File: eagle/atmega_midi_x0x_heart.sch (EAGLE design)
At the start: 31 parts, among them IC1 TL072P, J11_VCF_CUTOFF 22-23-2021, U1 ATMEGA328P_PDIP

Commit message: nearly routed
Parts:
- C1, C2: device rcl:C-US025-040X050 -> rcl:C-US050-024X044
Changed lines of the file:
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@@
 <grid distance="0.1" unitdist="inch" unit="inch" style="lines" multiple="1" display="no" altdistance="0.01" altunitdist="inch" altunit="inch"/>
 <layers>
-<layer number="1" name="Top" color="4" fill="1" visible="no" active="no"/>
-<layer number="16" name="Bottom" color="1" fill="1" visible="no" active="no"/>
-<layer number="17" name="Pads" color="2" fill="1" visible="no" active="no"/>
-<layer number="18" name="Vias" color="2" fill="1" visible="no" active="no"/>
-<layer number="19" name="Unrouted" color="6" fill="1" visible="no" active="no"/>
-<layer number="20" name="Dimension" color="15" fill="1" visible="no" active="no"/>
-<layer number="21" name="tPlace" color="7" fill="1" visible="no" active="no"/>
-<layer number="22" name="bPlace" color="7" fill="1" visible="no" active="no"/>
-<layer number="23" name="tOrigins" color="15" fill="1" visible="no" active="no"/>
-<layer number="24" name="bOrigins" color="15" fill="1" visible="no" active="no"/>
-<layer number="25" name="tNames" color="7" fill="1" visible="no" active="no"/>
-<layer number="26" name="bNames" color="7" fill="1" visible="no" active="no"/>
-<layer number="27" name="tValues" color="7" fill="1" visible="no" active="no"/>
-<layer number="28" name="bValues" color="7" fill="1" visible="no" active="no"/>
+<layer number="1" name="Top" color="4" fill="1" visible="yes" active="no"/>
+<layer number="16" name="Bottom" color="1" fill="1" visible="yes" active="no"/>
+<layer number="17" name="Pads" color="2" fill="1" visible="yes" active="no"/>
+<layer number="18" name="Vias" color="2" fill="1" visible="yes" active="no"/>
+<layer number="19" name="Unrouted" color="6" fill="1" visible="yes" active="no"/>
+<layer number="20" name="Dimension" color="15" fill="1" visible="yes" active="no"/>
+<layer number="21" name="tPlace" color="7" fill="1" visible="yes" active="no"/>
+<layer number="22" name="bPlace" color="7" fill="1" visible="yes" active="no"/>
+<layer number="23" name="tOrigins" color="15" fill="1" visible="yes" active="no"/>
+<layer number="24" name="bOrigins" color="15" fill="1" visible="yes" active="no"/>
+<layer number="25" name="tNames" color="7" fill="1" visible="yes" active="no"/>
+<layer number="26" name="bNames" color="7" fill="1" visible="yes" active="no"/>
+<layer number="27" name="tValues" color="7" fill="1" visible="yes" active="no"/>
+<layer number="28" name="bValues" color="7" fill="1" visible="yes" active="no"/>
 <layer number="29" name="tStop" color="7" fill="3" visible="no" active="no"/>
 <layer number="30" name="bStop" color="7" fill="6" visible="no" active="no"/>
@@
 <layer number="35" name="tGlue" color="7" fill="4" visible="no" active="no"/>
 <layer number="36" name="bGlue" color="7" fill="5" visible="no" active="no"/>
-<layer number="37" name="tTest" color="7" fill="1" visible="no" active="no"/>
-<layer number="38" name="bTest" color="7" fill="1" visible="no" active="no"/>
+<layer number="37" name="tTest" color="7" fill="1" visible="yes" active="no"/>
+<layer number="38" name="bTest" color="7" fill="1" visible="yes" active="no"/>
 <layer number="39" name="tKeepout" color="4" fill="11" visible="no" active="no"/>
 <layer number="40" name="bKeepout" color="1" fill="11" visible="no" active="no"/>
@@
 <layer number="44" name="Drills" color="7" fill="1" visible="no" active="no"/>
 <layer number="45" name="Holes" color="7" fill="1" visible="no" active="no"/>
-<layer number="46" name="Milling" color="3" fill="1" visible="no" active="no"/>
-<layer number="47" name="Measures" color="7" fill="1" visible="no" active="no"/>
-<layer number="48" name="Document" color="7" fill="1" visible="no" active="no"/>
-<layer number="49" name="Reference" color="7" fill="1" visible="no" active="no"/>
-<layer number="50" name="dxf" color="7" fill="1" visible="no" active="no"/>
-<layer number="51" name="tDocu" color="7" fill="1" visible="no" active="no"/>
-<layer number="52" name="bDocu" color="7" fill="1" visible="no" active="no"/>
-<layer number="53" name="tGND_GNDA" color="7" fill="9" visible="no" active="no"/>
-<layer number="54" name="bGND_GNDA" color="1" fill="9" visible="no" active="no"/>
-<layer number="56" name="wert" color="7" fill="1" visible="no" active="no"/>
-<layer number="57" name="tCAD" color="7" fill="1" visible="no" active="no"/>
-<layer number="59" name="tCarbon" color="7" fill="1" visible="no" active="no"/>
-<layer number="60" name="bCarbon" color="7" fill="1" visible="no" active="no"/>
+<layer number="46" name="Milling" color="3" fill="1" visible="yes" active="no"/>
+<layer number="47" name="Measures" color="7" fill="1" visible="yes" active="no"/>
+<layer number="48" name="Document" color="7" fill="1" visible="yes" active="no"/>
+<layer number="49" name="Reference" color="7" fill="1" visible="yes" active="no"/>
+<layer number="50" name="dxf" color="7" fill="1" visible="yes" active="no"/>
+<layer number="51" name="tDocu" color="7" fill="1" visible="yes" active="no"/>
+<layer number="52" name="bDocu" color="7" fill="1" visible="yes" active="no"/>
+<layer number="53" name="tGND_GNDA" color="7" fill="9" visible="yes" active="no"/>
+<layer number="54" name="bGND_GNDA" color="1" fill="9" visible="yes" active="no"/>
+<layer number="56" name="wert" color="7" fill="1" visible="yes" active="no"/>
+<layer number="57" name="tCAD" color="7" fill="1" visible="yes" active="no"/>
+<layer number="59" name="tCarbon" color="7" fill="1" visible="yes" active="no"/>
+<layer number="60" name="bCarbon" color="7" fill="1" visible="yes" active="no"/>
 <layer number="90" name="Modules" color="5" fill="1" visible="yes" active="yes"/>
 <layer number="91" name="Nets" color="2" fill="1" visible="yes" active="yes"/>
@@
 <part name="U1" library="SparkFun-DigitalIC" deviceset="ATMEGA328P_PDIP" device=""/>
 <part name="Q1" library="crystal" deviceset="CRYSTAL" device="HC49S"/>
-<part name="C1" library="rcl" deviceset="C-US" device="025-040X050" value="27pF"/>
-<part name="C2" library="rcl" deviceset="C-US" device="025-040X050" value="27pF"/>
+<part name="C1" library="rcl" deviceset="C-US" device="050-024X044" value="27pF"/>
+<part name="C2" library="rcl" deviceset="C-US" device="050-024X044" value="27pF"/>
 <part name="R1" library="rcl" deviceset="R-US_" device="0207/10" value="10k"/>
 <part name="OK1" library="optocoupler" deviceset="6N138" device=""/>

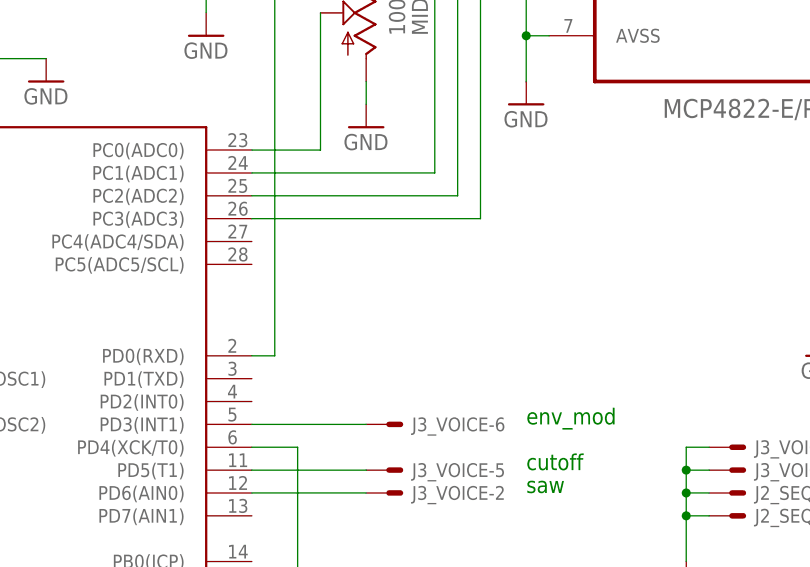
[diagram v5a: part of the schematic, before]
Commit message: setting up pin constants and added gate led
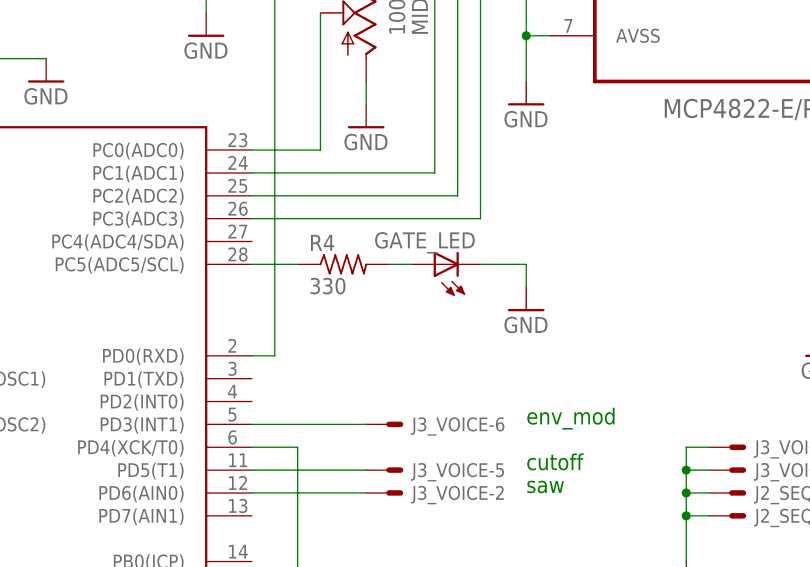
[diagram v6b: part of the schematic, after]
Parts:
- added GATE_LED: (no value), led:LED5MM
- added R4: 330, rcl:R-US_0207/10
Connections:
- new net N$24: GATE_LED.A, R4.2
- new net N$28: R4.1, U1.PC5(ADC5/SCL)
- net GND: now also GATE_LED.C
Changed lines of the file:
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@@
 <grid distance="0.1" unitdist="inch" unit="inch" style="lines" multiple="1" display="no" altdistance="0.01" altunitdist="inch" altunit="inch"/>
 <layers>
-<layer number="1" name="Top" color="4" fill="1" visible="yes" active="no"/>
-<layer number="16" name="Bottom" color="1" fill="1" visible="yes" active="no"/>
-<layer number="17" name="Pads" color="2" fill="1" visible="yes" active="no"/>
-<layer number="18" name="Vias" color="2" fill="1" visible="yes" active="no"/>
-<layer number="19" name="Unrouted" color="6" fill="1" visible="yes" active="no"/>
-<layer number="20" name="Dimension" color="15" fill="1" visible="yes" active="no"/>
-<layer number="21" name="tPlace" color="7" fill="1" visible="yes" active="no"/>
-<layer number="22" name="bPlace" color="7" fill="1" visible="yes" active="no"/>
-<layer number="23" name="tOrigins" color="15" fill="1" visible="yes" active="no"/>
-<layer number="24" name="bOrigins" color="15" fill="1" visible="yes" active="no"/>
-<layer number="25" name="tNames" color="7" fill="1" visible="yes" active="no"/>
-<layer number="26" name="bNames" color="7" fill="1" visible="yes" active="no"/>
-<layer number="27" name="tValues" color="7" fill="1" visible="yes" active="no"/>
-<layer number="28" name="bValues" color="7" fill="1" visible="yes" active="no"/>
+<layer number="1" name="Top" color="4" fill="1" visible="no" active="no"/>
+<layer number="16" name="Bottom" color="1" fill="1" visible="no" active="no"/>
+<layer number="17" name="Pads" color="2" fill="1" visible="no" active="no"/>
+<layer number="18" name="Vias" color="2" fill="1" visible="no" active="no"/>
+<layer number="19" name="Unrouted" color="6" fill="1" visible="no" active="no"/>
+<layer number="20" name="Dimension" color="15" fill="1" visible="no" active="no"/>
+<layer number="21" name="tPlace" color="7" fill="1" visible="no" active="no"/>
+<layer number="22" name="bPlace" color="7" fill="1" visible="no" active="no"/>
+<layer number="23" name="tOrigins" color="15" fill="1" visible="no" active="no"/>
+<layer number="24" name="bOrigins" color="15" fill="1" visible="no" active="no"/>
+<layer number="25" name="tNames" color="7" fill="1" visible="no" active="no"/>
+<layer number="26" name="bNames" color="7" fill="1" visible="no" active="no"/>
+<layer number="27" name="tValues" color="7" fill="1" visible="no" active="no"/>
+<layer number="28" name="bValues" color="7" fill="1" visible="no" active="no"/>
 <layer number="29" name="tStop" color="7" fill="3" visible="no" active="no"/>
 <layer number="30" name="bStop" color="7" fill="6" visible="no" active="no"/>
@@
 <layer number="35" name="tGlue" color="7" fill="4" visible="no" active="no"/>
 <layer number="36" name="bGlue" color="7" fill="5" visible="no" active="no"/>
-<layer number="37" name="tTest" color="7" fill="1" visible="yes" active="no"/>
-<layer number="38" name="bTest" color="7" fill="1" visible="yes" active="no"/>
+<layer number="37" name="tTest" color="7" fill="1" visible="no" active="no"/>
+<layer number="38" name="bTest" color="7" fill="1" visible="no" active="no"/>
 <layer number="39" name="tKeepout" color="4" fill="11" visible="no" active="no"/>
 <layer number="40" name="bKeepout" color="1" fill="11" visible="no" active="no"/>
@@
 <layer number="44" name="Drills" color="7" fill="1" visible="no" active="no"/>
 <layer number="45" name="Holes" color="7" fill="1" visible="no" active="no"/>
-<layer number="46" name="Milling" color="3" fill="1" visible="yes" active="no"/>
-<layer number="47" name="Measures" color="7" fill="1" visible="yes" active="no"/>
-<layer number="48" name="Document" color="7" fill="1" visible="yes" active="no"/>
-<layer number="49" name="Reference" color="7" fill="1" visible="yes" active="no"/>
-<layer number="50" name="dxf" color="7" fill="1" visible="yes" active="no"/>
-<layer number="51" name="tDocu" color="7" fill="1" visible="yes" active="no"/>
-<layer number="52" name="bDocu" color="7" fill="1" visible="yes" active="no"/>
-<layer number="53" name="tGND_GNDA" color="7" fill="9" visible="yes" active="no"/>
-<layer number="54" name="bGND_GNDA" color="1" fill="9" visible="yes" active="no"/>
-<layer number="56" name="wert" color="7" fill="1" visible="yes" active="no"/>
-<layer number="57" name="tCAD" color="7" fill="1" visible="yes" active="no"/>
-<layer number="59" name="tCarbon" color="7" fill="1" visible="yes" active="no"/>
-<layer number="60" name="bCarbon" color="7" fill="1" visible="yes" active="no"/>
+<layer number="46" name="Milling" color="3" fill="1" visible="no" active="no"/>
+<layer number="47" name="Measures" color="7" fill="1" visible="no" active="no"/>
+<layer number="48" name="Document" color="7" fill="1" visible="no" active="no"/>
+<layer number="49" name="Reference" color="7" fill="1" visible="no" active="no"/>
+<layer number="50" name="dxf" color="7" fill="1" visible="no" active="no"/>
+<layer number="51" name="tDocu" color="7" fill="1" visible="no" active="no"/>
+<layer number="52" name="bDocu" color="7" fill="1" visible="no" active="no"/>
+<layer number="53" name="tGND_GNDA" color="7" fill="9" visible="no" active="no"/>
+<layer number="54" name="bGND_GNDA" color="1" fill="9" visible="no" active="no"/>
+<layer number="56" name="wert" color="7" fill="1" visible="no" active="no"/>
+<layer number="57" name="tCAD" color="7" fill="1" visible="no" active="no"/>
+<layer number="59" name="tCarbon" color="7" fill="1" visible="no" active="no"/>
+<layer number="60" name="bCarbon" color="7" fill="1" visible="no" active="no"/>
 <layer number="90" name="Modules" color="5" fill="1" visible="yes" active="yes"/>
 <layer number="91" name="Nets" color="2" fill="1" visible="yes" active="yes"/>
@@
 <part name="GND10" library="supply1" deviceset="GND" device=""/>
 <part name="GND11" library="supply1" deviceset="GND" device=""/>
+<part name="R4" library="rcl" deviceset="R-US_" device="0207/10" value="330"/>
+<part name="GATE_LED" library="led" deviceset="LED" device="5MM"/>
+<part name="GND12" library="supply1" deviceset="GND" device=""/>
 </parts>
 <sheets>
@@
 <instance part="GND10" gate="1" x="142.24" y="50.8"/>
 <instance part="GND11" gate="1" x="121.92" y="78.74"/>
+<instance part="R4" gate="G$1" x="53.34" y="60.96"/>
+<instance part="GATE_LED" gate="G$1" x="63.5" y="60.96" rot="R90"/>
+<instance part="GND12" gate="1" x="73.66" y="55.88"/>
 </instances>
 <busses>
@@
 <pinref part="GND11" gate="1" pin="GND"/>
 </segment>
-</net>
+<segment>
+<pinref part="GATE_LED" gate="G$1" pin="C"/>
+<pinref part="GND12" gate="1" pin="GND"/>
+<wire x1="68.58" y1="60.96" x2="73.66" y2="60.96" width="0.1524" layer="91"/>
+<wire x1="73.66" y1="60.96" x2="73.66" y2="58.42" width="0.1524" layer="91"/>
+</segment>
+</net>
+<net name="N$24" class="0">
+<segment>
+<pinref part="R4" gate="G$1" pin="2"/>
+<pinref part="GATE_LED" gate="G$1" pin="A"/>
+<wire x1="60.96" y1="60.96" x2="58.42" y2="60.96" width="0.1524" layer="91"/>
+</segment>
+</net>
+<net name="N$28" class="0">
+<segment>
+<pinref part="U1" gate="G$1" pin="PC5(ADC5/SCL)"/>
+<pinref part="R4" gate="G$1" pin="1"/>
+<wire x1="48.26" y1="60.96" x2="43.18" y2="60.96" width="0.1524" layer="91"/>
+</segment>
+</net>
